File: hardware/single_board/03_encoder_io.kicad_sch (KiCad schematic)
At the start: 36 parts, among them J12 USB-C, J13 EXPANSION, J14 RS485 IN, J15 RS485 OUT, SW1 BOOTSEL, U13 USBLC6-2SC6, U14 SIT3088ETK, U15 SIT3088ETK, U17 SIT3088ETK, U18 SIT3088ETK

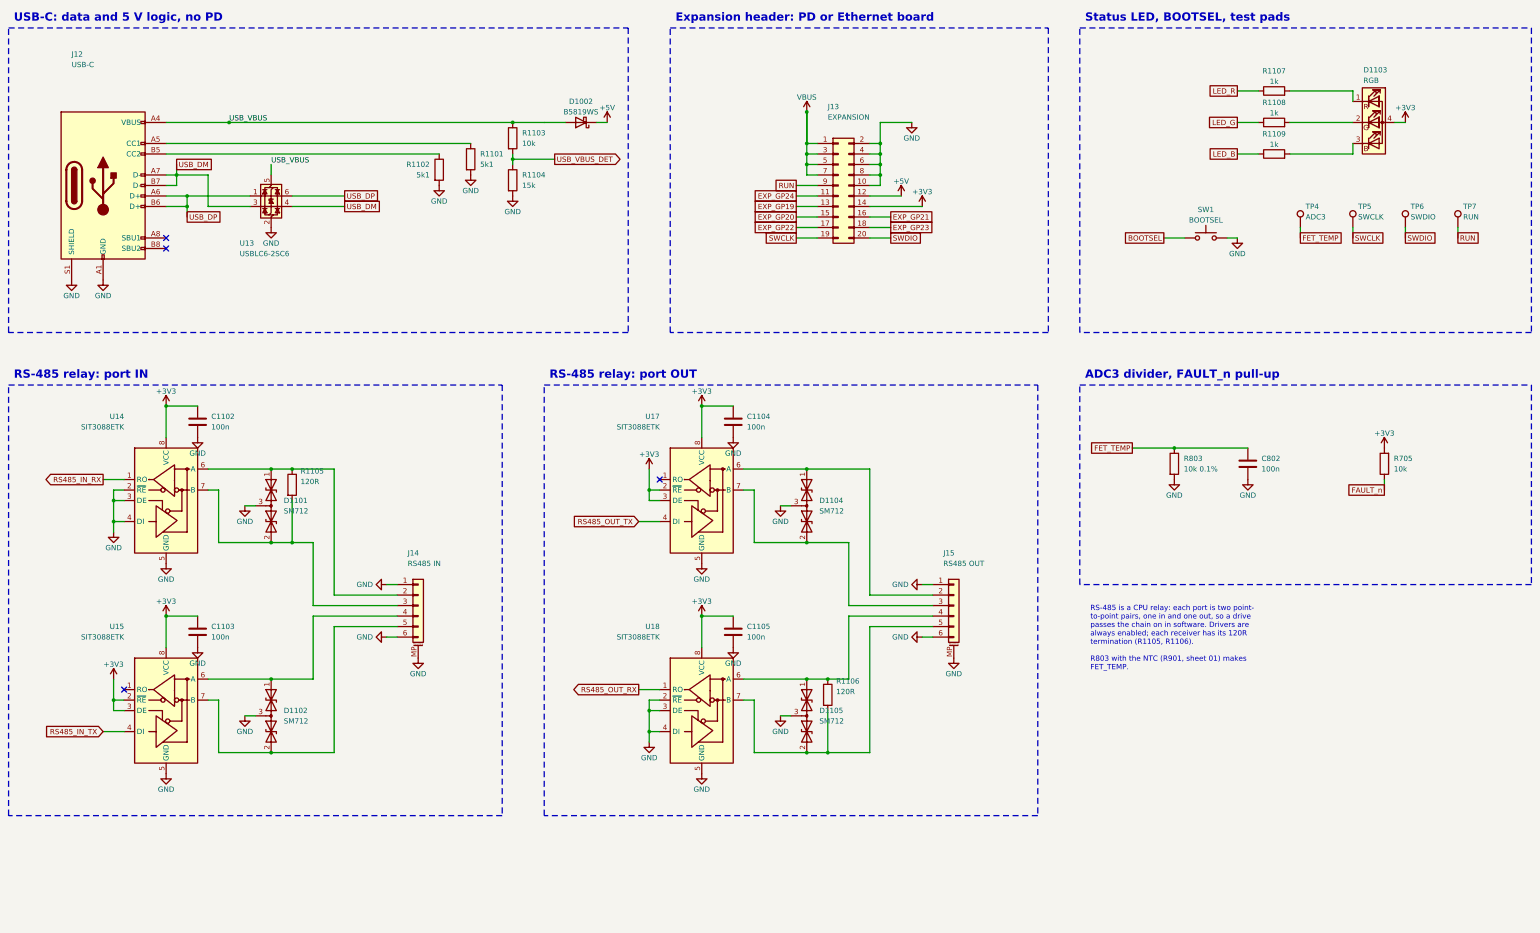
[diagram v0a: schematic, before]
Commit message: Board S schematic on three sheets: bridge + CPU, power, encoder + IO
Asked for fewer pages: the power bridge goes with the CPU that drives it
(A2), the encoder with the rest of the IO (A3); the supplies keep their
sheet. schematic_s.SHEET_OF maps the parts' sheet names (board A keeps its
own), and schdraw.Sheet.origin() lets a sheet place layouts written in their
own coordinates side by side. HIN/LIN and the other CPU-to-bridge nets are
now local labels on one sheet. The notes say which sheet a part is on.

KiCad's netlist matches schematic_s.nets(); ERC 0. The board is linked to
the netlist by reference, so the PCB is untouched.

Co-Authored-By: Claude Opus 5.5 (1M context) <noreply@anthropic.com>
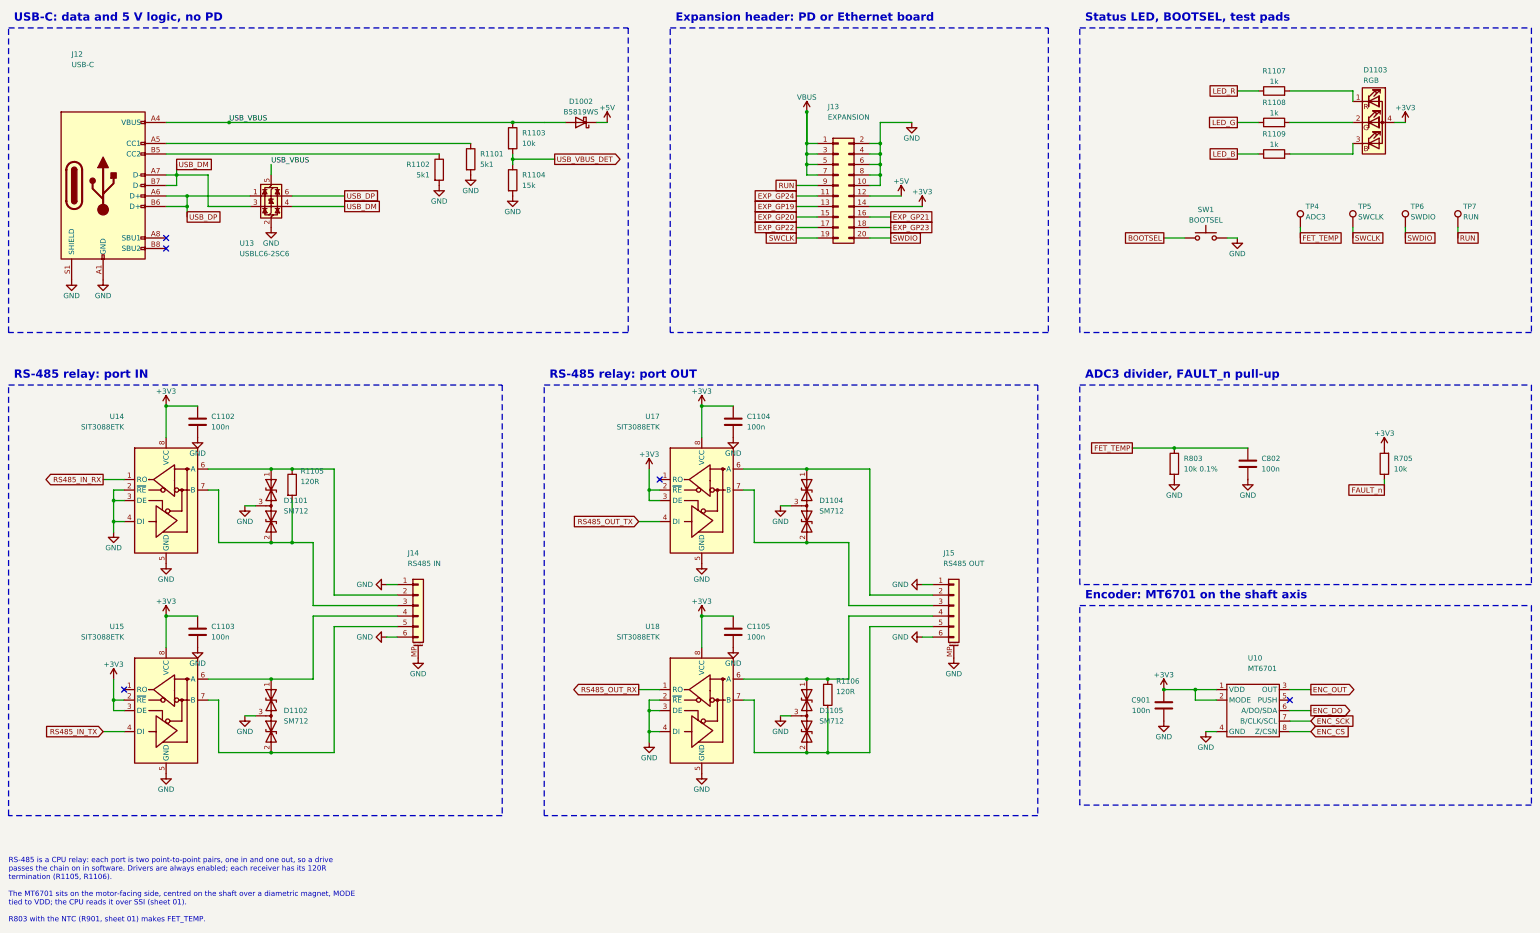
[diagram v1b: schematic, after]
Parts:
- added C901: 100n, Capacitor_SMD:C_0402_1005Metric, symbol Device:C
- added U10: MT6701, Package_SO:SOIC-8_3.9x4.9mm_P1.27mm, symbol servodrive:MT6701
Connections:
- net +3V3: now also C901.1, U10.1 (VDD), U10.2 (MODE)
- net GND: now also C901.2, U10.4 (GND)
- new net ENC_CS: U10.8 (Z/CSN)
- new net ENC_DO: U10.6 (A/DO/SDA)
- new net ENC_OUT: U10.3 (OUT)
- new net ENC_SCK: U10.7 (B/CLK/SCL)
- no-connect marks 4 -> 5
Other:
- note added: "Encoder: MT6701 on the shaft axis"
- note added: "RS-485 is a CPU relay: each port is two point-to-point pairs, one in and one out, so a drive passes the chain on in software. Drivers are always enabled; each receiver has its 120R termination (R1105, R1106). The MT6701 sits on the motor-facing side, centred on the shaft over a diametric magnet, MODE tied to VDD; the CPU reads it over SSI (sheet 01). R803 with the NTC (R901, sheet 01) makes FET_T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"
- note removed: "RS-485 is a CPU relay: each port is two point- to-point pairs, one in and one out, so a drive passes the chain on in software. Drivers are always enabled; each receiver has its 120R termination (R1105, R1106). R803 with the NTC (R901, sheet 01) makes FET_TEMP."
- title: servodrive — board S, single board — 05_io -> servodrive — board S, single board — 03_encoder_io

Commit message: Board S: SIT65HVD75ETK and W25Q80DVUXIE for the parts that went out of stock
Every placed part re-checked at JLCPCB on 2026-10-16: the SIT3088ETK and
the W25Q16JVUXIQ were at zero. The SIT65HVD75ETK is the same MAX3485
pinout in the same DFN-8 3x3 (C7433976, 20,671 in stock), and its receiver
threshold (V_IT+ <= -10 mV) reads a terminated idle pair as a 1, which
answers the fail-safe item on paper. The W25Q80DVUXIE is the same pins and
USON 2x3 land pattern, 8 Mbit (C401667, 8,611): firmware needs
PICO_FLASH_SIZE_BYTES 1 MB and has to set QE, which it ships clear.

Board S only (schematic_s overrides; board A keeps the W25Q16JV): two new
derived symbols appended to the library, the two sheets regenerated, the
routed board's value fields patched, the fan-out's escape rule taking the
new name. ERC 0, netlist == schematic_s, DRC 0 / 0 unconnected, schematic
parity the same 219 items as before. Viewer rebuilt.

Still short: the RP2350's 3.3 uH AOTA-B201610S3R3 (9) and TPSMF4L54A (42,
three a board).

Co-Authored-By: Claude Opus 5.5 <noreply@anthropic.com>
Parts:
- U14, U15, U17, U18: value SIT3088ETK -> SIT65HVD75ETK; symbol servodrive:SIT3088 -> servodrive:SIT65HVD75
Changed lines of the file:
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@@
 	)
 	(symbol
-		(lib_id "servodrive:SIT3088")
+		(lib_id "servodrive:SIT65HVD75")
 		(at 58.4200 138.4300 0)
 		(unit 1)
@@
 			(at 48.2600 118.1100 0)
 			(effects (font (size 1.27 1.27)) (justify right)))
-		(property "Value" "SIT3088ETK"
+		(property "Value" "SIT65HVD75ETK"
 			(at 48.2600 120.6500 0)
 			(effects (font (size 1.27 1.27)) (justify right)))
@@
 	)
 	(symbol
-		(lib_id "servodrive:SIT3088")
+		(lib_id "servodrive:SIT65HVD75")
 		(at 58.4200 189.2300 0)
 		(unit 1)
@@
 			(at 48.2600 168.9100 0)
 			(effects (font (size 1.27 1.27)) (justify right)))
-		(property "Value" "SIT3088ETK"
+		(property "Value" "SIT65HVD75ETK"
 			(at 48.2600 171.4500 0)
 			(effects (font (size 1.27 1.27)) (justify right)))
@@
 	)
 	(symbol
-		(lib_id "servodrive:SIT3088")
+		(lib_id "servodrive:SIT65HVD75")
 		(at 187.9600 138.4300 0)
 		(unit 1)
@@
 			(at 177.8000 118.1100 0)
 			(effects (font (size 1.27 1.27)) (justify right)))
-		(property "Value" "SIT3088ETK"
+		(property "Value" "SIT65HVD75ETK"
 			(at 177.8000 120.6500 0)
 			(effects (font (size 1.27 1.27)) (justify right)))
@@
 	)
 	(symbol
-		(lib_id "servodrive:SIT3088")
+		(lib_id "servodrive:SIT65HVD75")
 		(at 187.9600 189.2300 0)
 		(unit 1)
@@
 			(at 177.8000 168.9100 0)
 			(effects (font (size 1.27 1.27)) (justify right)))
-		(property "Value" "SIT3088ETK"
+		(property "Value" "SIT65HVD75ETK"
 			(at 177.8000 171.4500 0)
 			(effects (font (size 1.27 1.27)) (justify right)))
